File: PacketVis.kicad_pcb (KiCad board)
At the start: 2 copper layers, 59 x 44.5 mm, 36 parts, among them J1 USB_B_Micro, J2 Conn_01x03, SW1 SW_Push_Dual, SW2 SW_SPST, SW3 SW_SPST, U1 3.3V 1A, U2 74HC595, U3 ESP-WROOM-02D

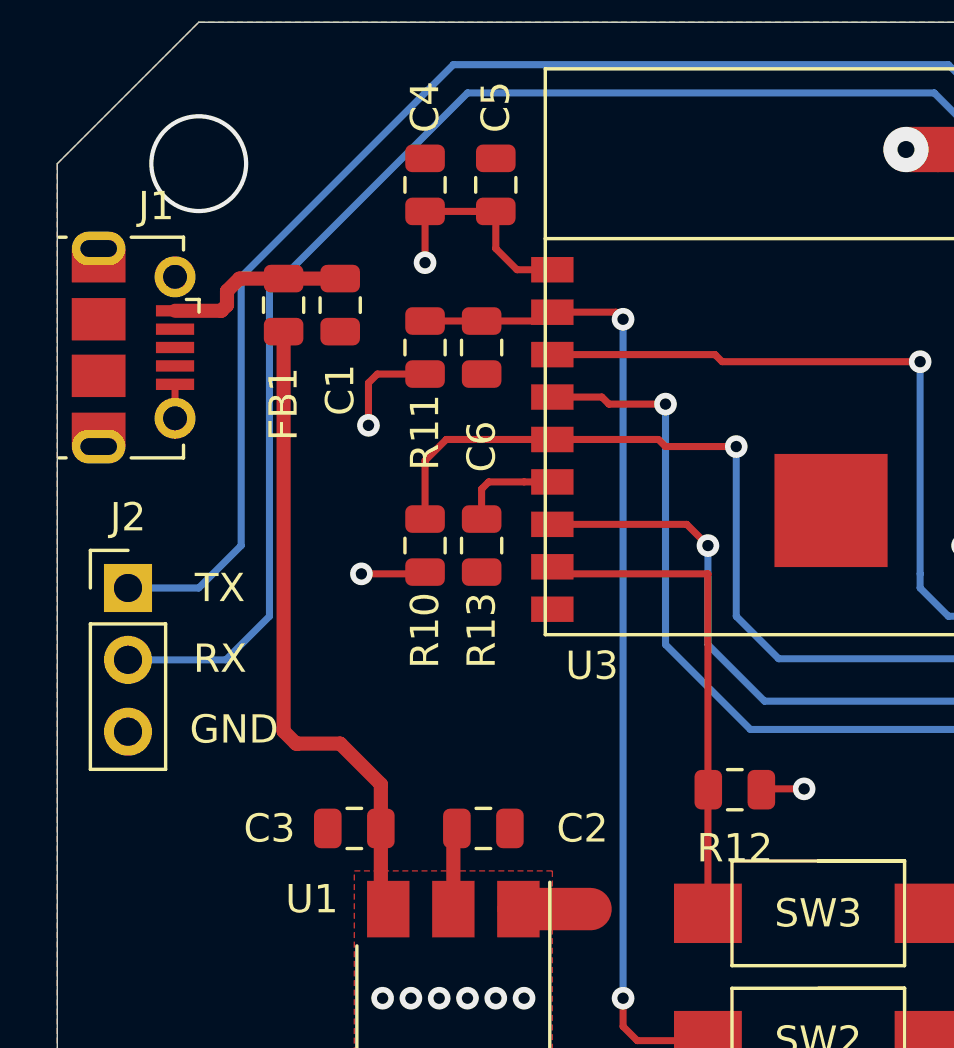
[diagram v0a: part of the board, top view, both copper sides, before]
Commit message: Update Silkscreen
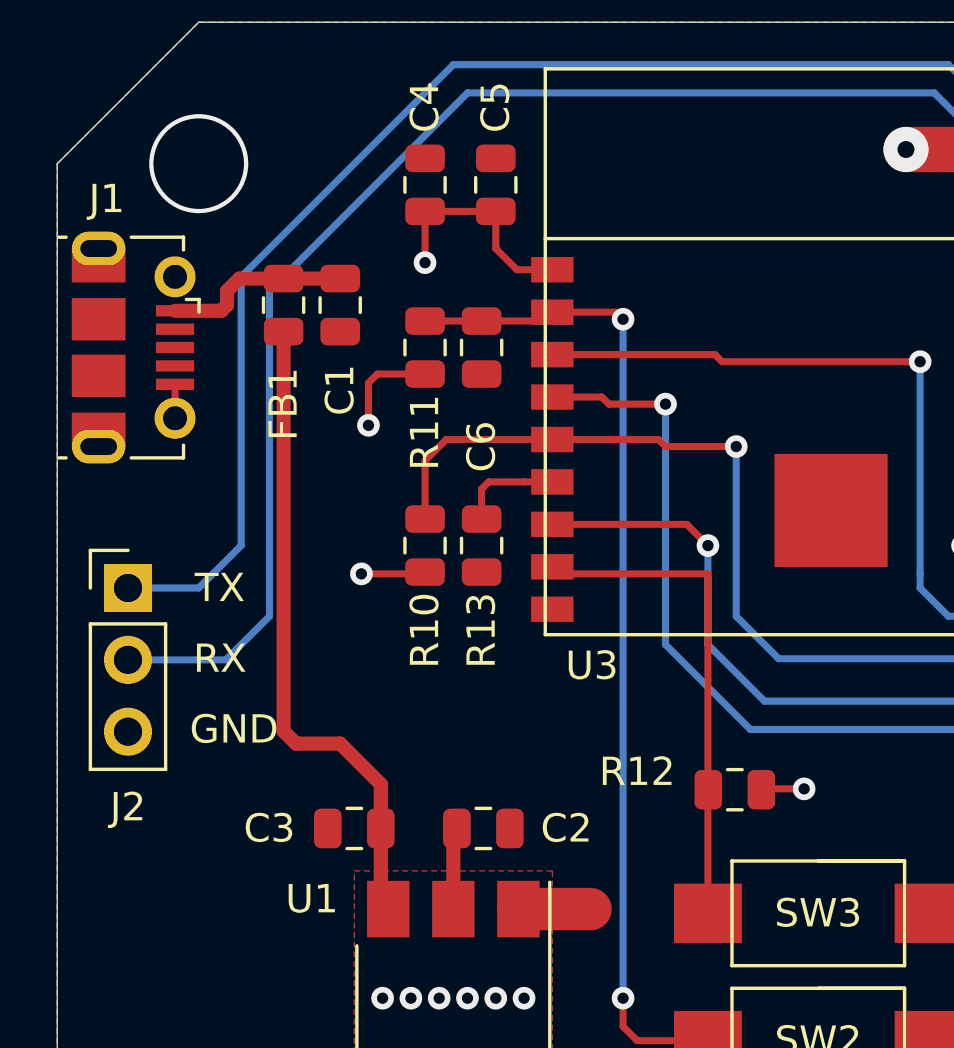
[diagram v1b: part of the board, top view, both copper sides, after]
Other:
- board text added: "PacketVis Revision A02"
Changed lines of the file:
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@@
   (general
     (thickness 1.6)
-    (drawings 15)
+    (drawings 16)
     (tracks 245)
     (zones 0)
@@
     (tags resistor)
     (attr smd)
-    (fp_text reference R12 (at 0 -2.07) (layer F.SilkS)
+    (fp_text reference R12 (at 3.45 0.63) (layer F.SilkS)
       (effects (font (size 1 1) (thickness 0.15)))
     )
@@
     (descr "Through hole straight pin header, 1x03, 2.54mm pitch, single row")
     (tags "Through hole pin header THT 1x03 2.54mm single row")
-    (fp_text reference J2 (at 0 -2.5) (layer F.SilkS)
+    (fp_text reference J2 (at 0 7.75) (layer F.SilkS)
       (effects (font (size 1 1) (thickness 0.15)))
     )
@@
     (tags "Micro-USB SMD Typ-B")
     (attr smd)
-    (fp_text reference J1 (at -5 -0.8 180) (layer F.SilkS)
+    (fp_text reference J1 (at -5.25 0.95 180) (layer F.SilkS)
       (effects (font (size 1 1) (thickness 0.15)))
     )
@@
     (tags capacitor)
     (attr smd)
-    (fp_text reference C2 (at 3.5 0) (layer F.SilkS)
+    (fp_text reference C2 (at 2.9375 0) (layer F.SilkS)
       (effects (font (size 1 1) (thickness 0.15)))
     )
@@
     )
   )
+  (gr_text "PacketVis Revision A02" (at 222.18 115.5) (layer F.Mask)
+    (effects (font (size 1.25 1.35) (thickness 0.15)))
+  )
   (gr_circle (center 187.18 79) (end 188.18 79) (layer F.Mask) (width 2))

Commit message: Update Routing
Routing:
- net /ESP_RX: track 63.3 -> 37.3 mm
- net /ESP_TX: track 61.0 -> 35.1 mm
- net +3V3: track 49.0 -> 43.2 mm, vias 14 -> 12
- net /OUTPUT_ENABLE: track 49.1 -> 44.6 mm
- net /SW_1: track 55.2 -> 52.0 mm
- net /CLOCK: track 40.0 -> 37.1 mm
- net /LATCH: track 23.7 -> 22.8 mm
- net /CLEAR: track 45.3 -> 44.8 mm
- net /BOOT: vias 0 -> 2

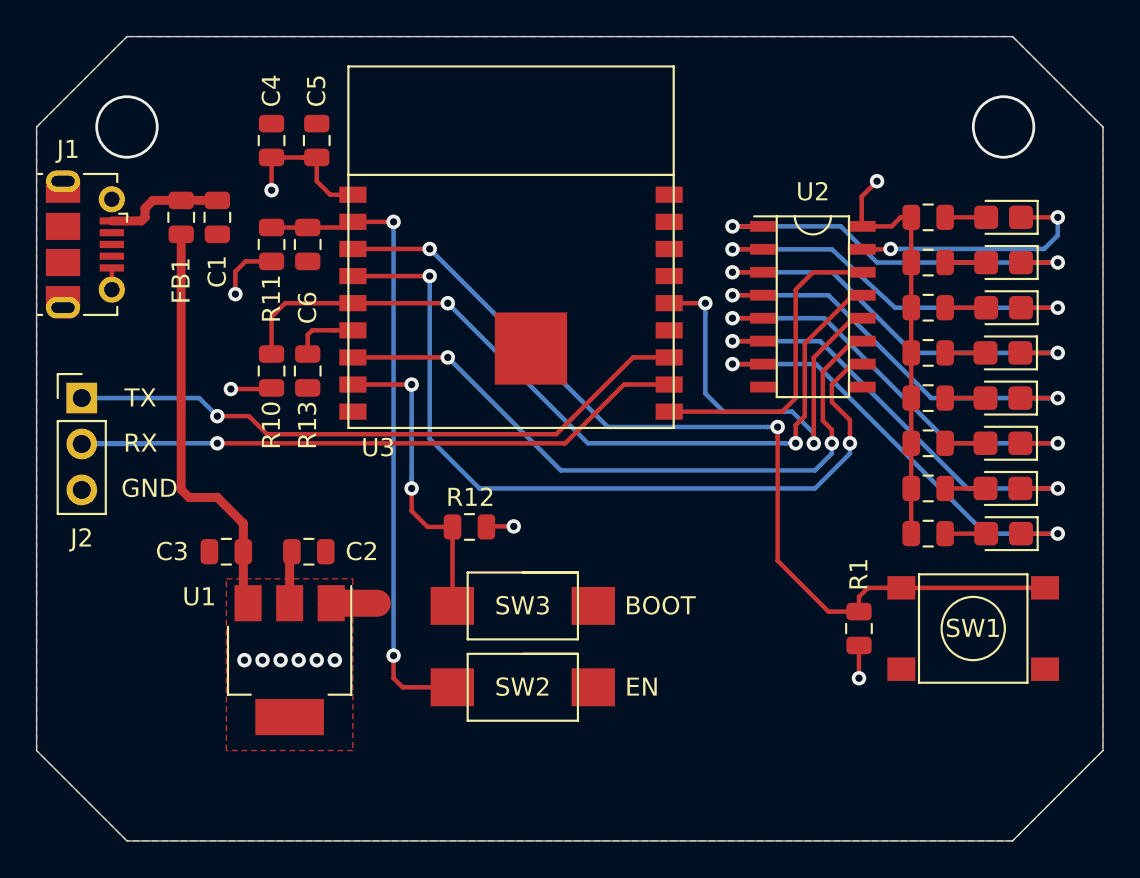
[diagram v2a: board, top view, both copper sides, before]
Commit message: Add 5V to Programming Header
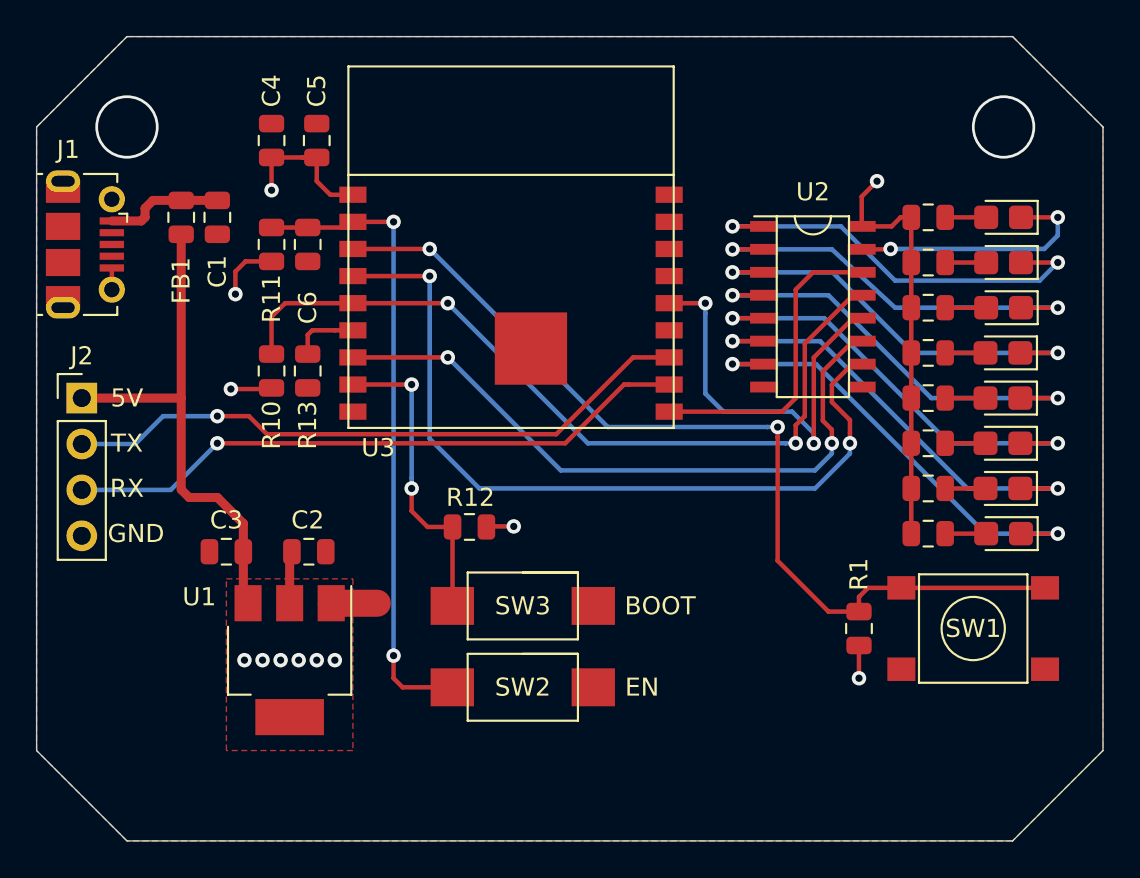
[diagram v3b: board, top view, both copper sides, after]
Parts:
- J2: value Conn_01x03 -> Conn_01x04; footprint Connector_PinHeader_2.54mm:PinHeader_1x03_P2.54mm_Vertical -> Connector_PinHeader_2.54mm:PinHeader_1x04_P2.54mm_Vertical
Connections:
- J2 pad 1: /ESP_TX -> +5V
- J2 pad 2: /ESP_RX -> /ESP_TX
- J2 pad 3: GND -> /ESP_RX
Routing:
- net +5V: track 22.9 -> 28.4 mm
- net /ESP_RX: track 37.3 -> 34.9 mm
- net /LED_2: track 22.6 -> 23.4 mm
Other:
- board text added: "5V"

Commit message: Changed U2 to 5v TTL Shift Register needs 5V instead of previous 3.3V Traces rerouted Added PCBA Step File
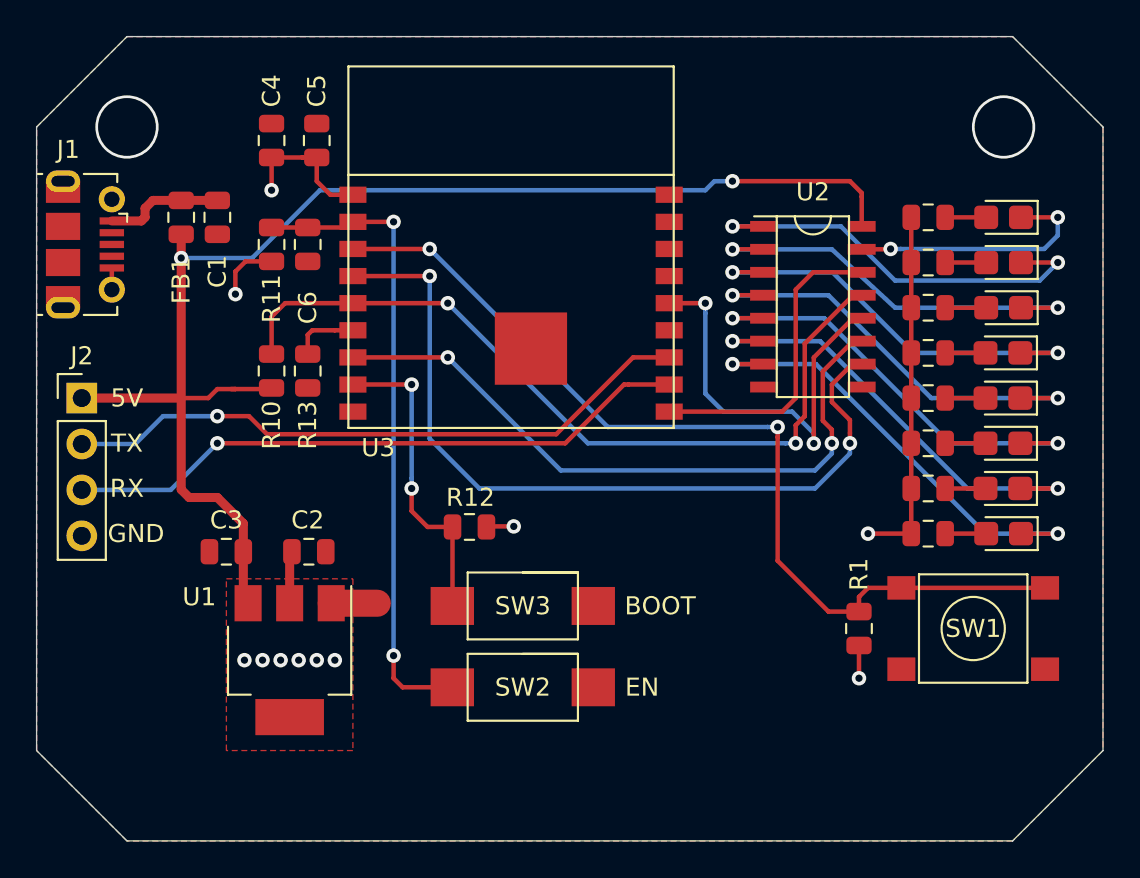
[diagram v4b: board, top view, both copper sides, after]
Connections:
- R10 pad 1: +3V3 -> +5V
- U2 pad 16: +3V3 -> +5V
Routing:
- net +5V: track 28.4 -> 75.4 mm, vias 0 -> 2
- net +3V3: track 43.2 -> 37.6 mm, vias 12 -> 11
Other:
- board text added: "JLCJLCJLCJLC"
- board text added: "PacketVis REV: A02"
- board text removed: "PacketVis Revision A02"
